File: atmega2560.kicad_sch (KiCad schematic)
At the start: 7 parts, among them SW1701 SW_SPST, U1701 ATmega2560-16A, U1702 HEADER_3x2, Y1701 crystal_arduino

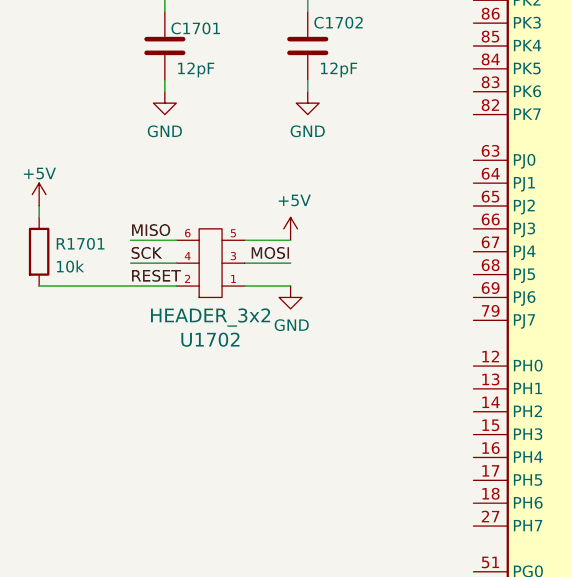
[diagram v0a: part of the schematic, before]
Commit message: added ch340.sch
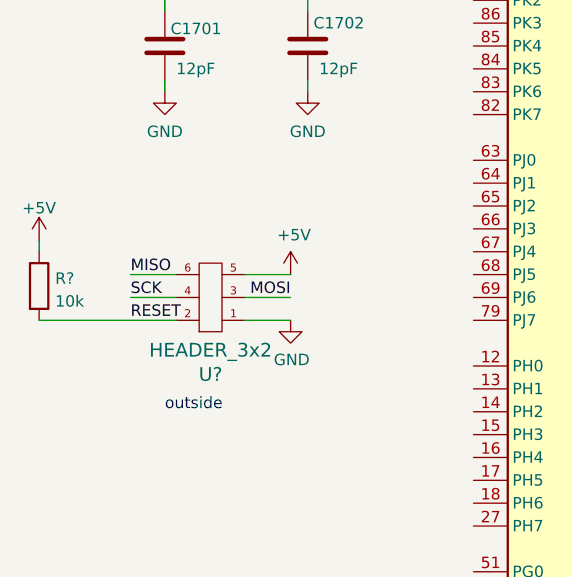
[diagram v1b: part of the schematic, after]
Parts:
- removed R1701: 10k, Resistor_SMD:R_1206_3216Metric_Pad1.30x1.75mm_HandSolder, symbol Device:R
- removed U1702: HEADER_3x2, Connector_PinSocket_1.27mm:PinSocket_2x03_P1.27mm_Vertical, symbol servoDriverSMD-rescue:HEADER_3x2-w_connectors
- added R?: 10k, Resistor_SMD:R_0603_1608Metric_Pad0.98x0.95mm_HandSolder, symbol Device:R
- added U?: HEADER_3x2, Connector_PinSocket_1.27mm:PinSocket_2x03_P1.27mm_Vertical, symbol servoDriverSMD-rescue:HEADER_3x2-w_connectors
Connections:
- net +5V: now also R?.1, U?.5
- net GND: now also U?.1
- net MISO: now also U?.6
- net MOSI: now also U?.3
- net RESET: now also R?.2, U?.2
- net SCK: now also U?.4
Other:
- note added: "outside"

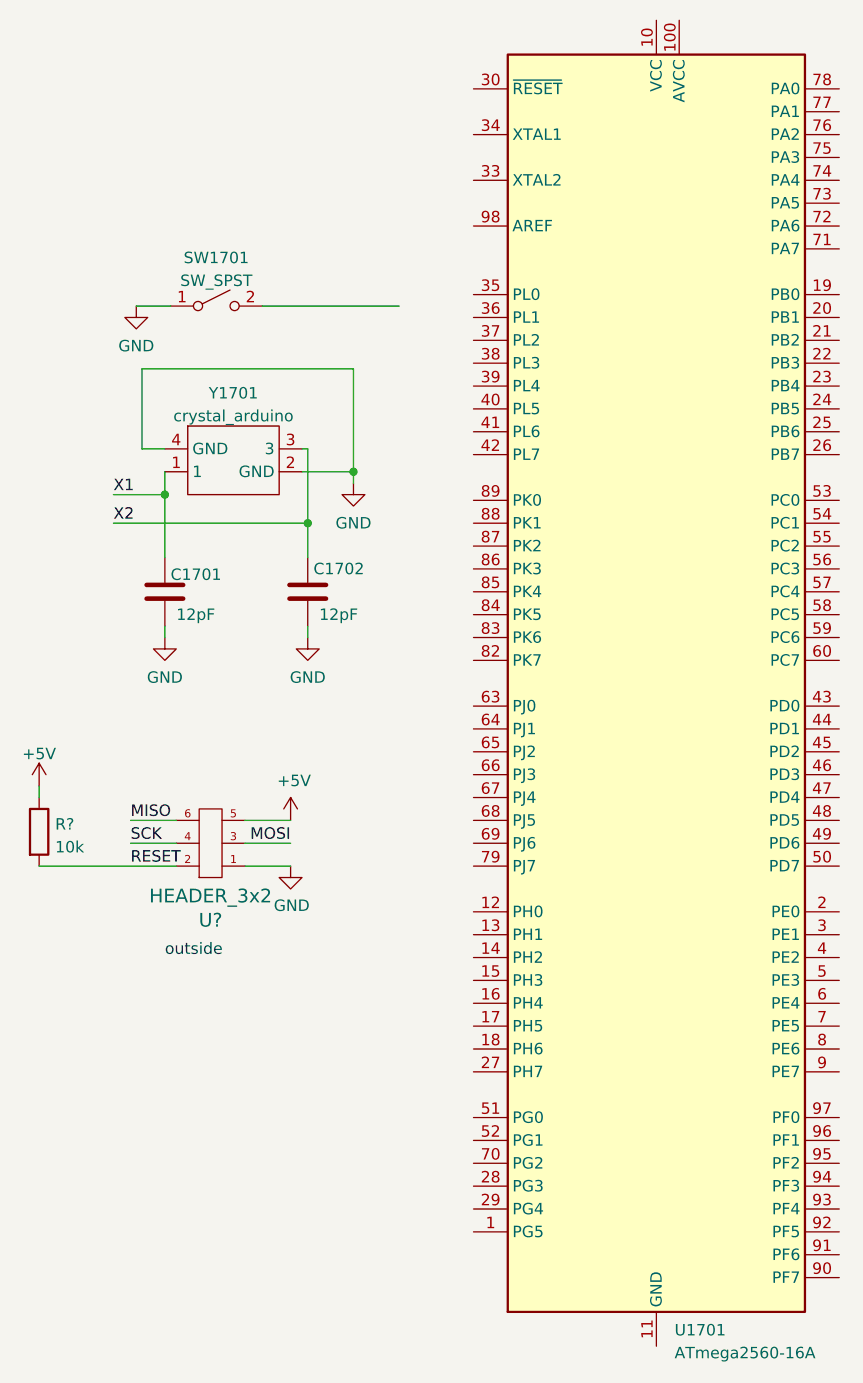
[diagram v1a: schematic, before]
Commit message: added hierarchial labels to some schematics
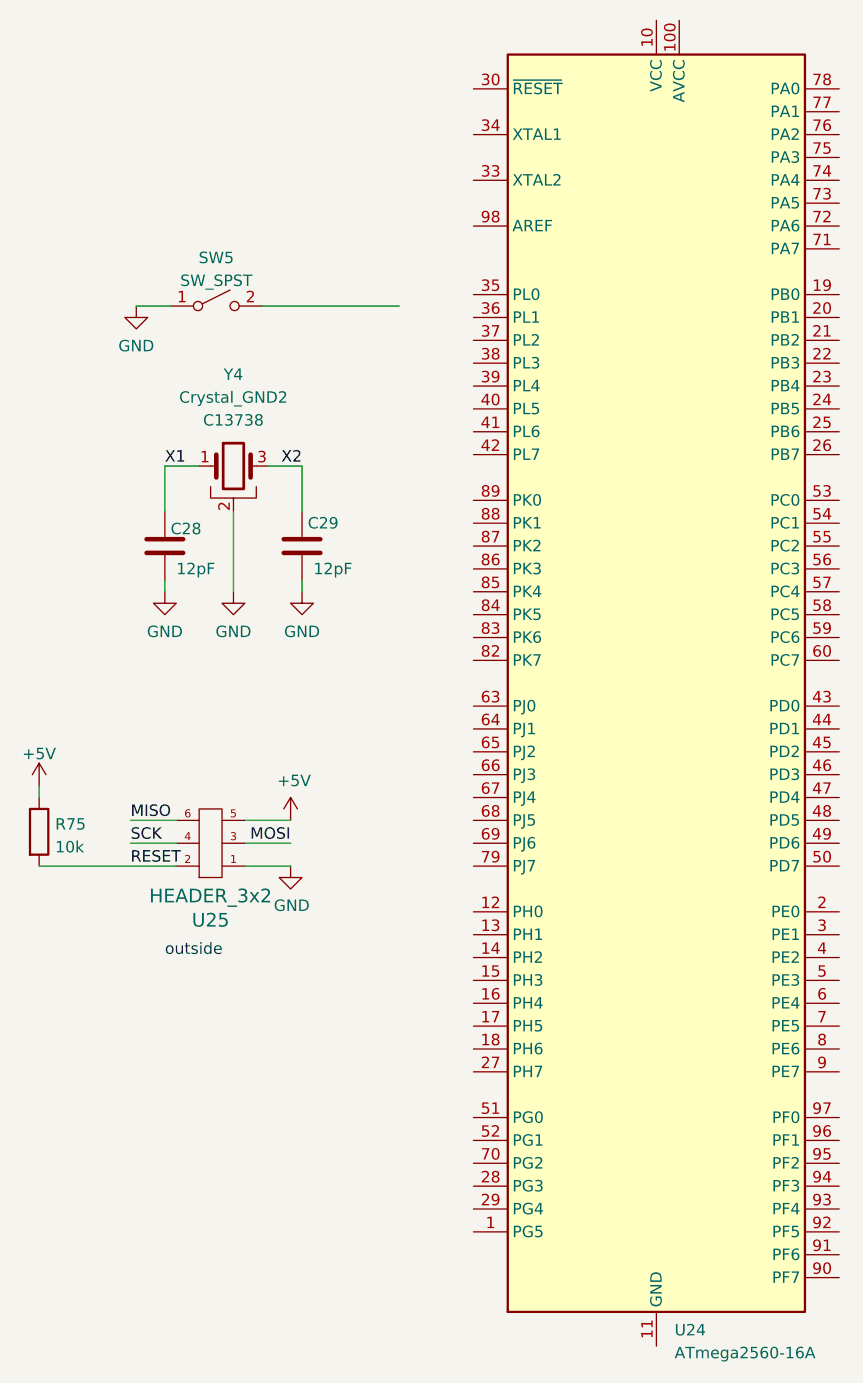
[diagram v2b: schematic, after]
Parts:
- removed Y1701: crystal_arduino, custom_kicad_lib_sk:crystal_arduino, symbol custom_bas:crystal_arduino
- added Y4: Crystal_GND2, custom_kicad_lib_sk:crystal_arduino, symbol custom_kicad_lib_sk:crystal_arduino
- gave numbers to parts that had none: 2
- renumbered C1701 to C28, C1702 to C29, SW1701 to SW5, U1701 to U24
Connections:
- net GND: now also Y4.2 (GND), Y4.4 (GND)
- net X1: now also Y4.1
- net X2: now also Y4.3
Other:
- moved on the sheet: C28, C29

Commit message: moved some schematic scheets to their own folders and routed a board with it. This allow for re-use of PCB parts.
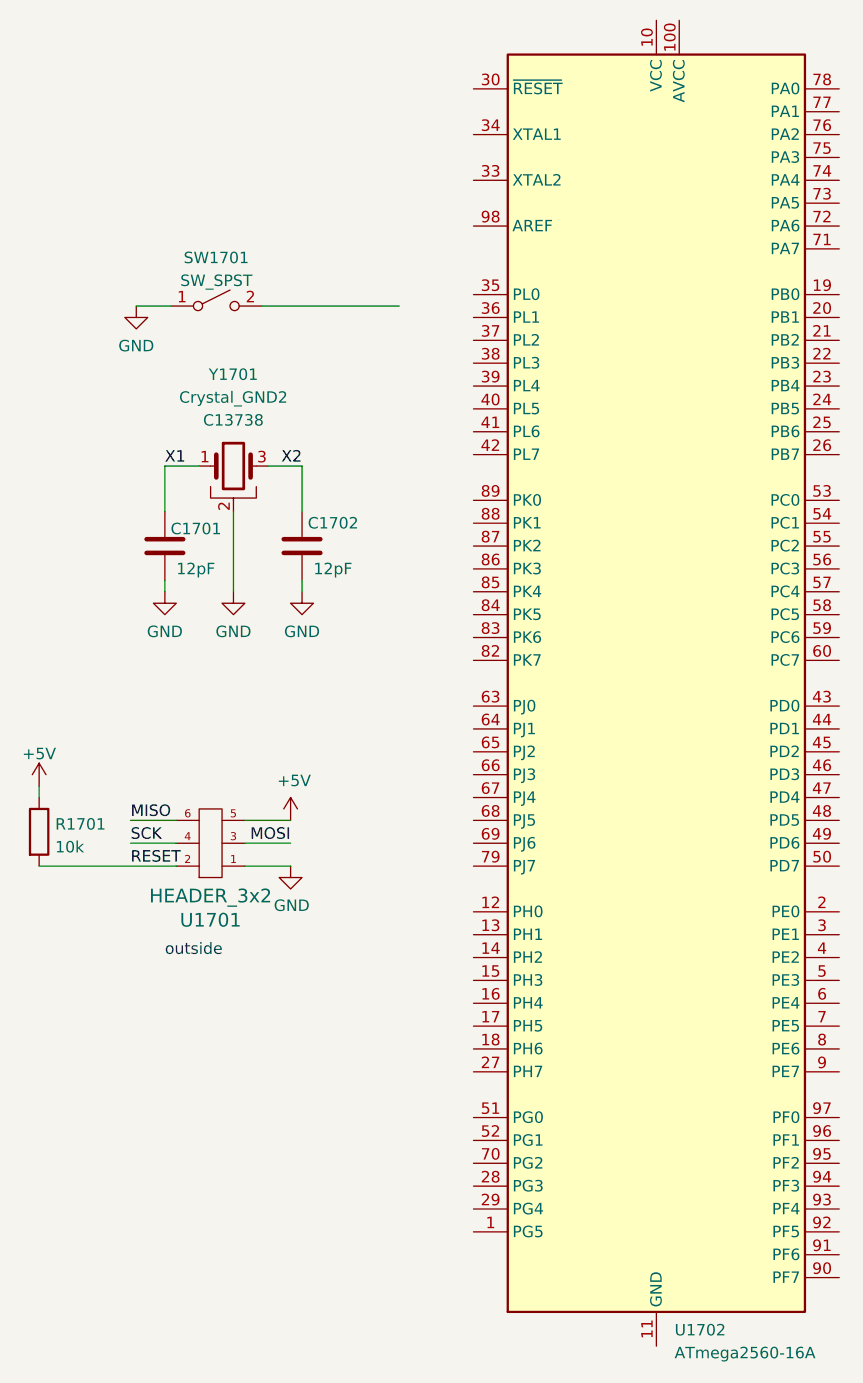
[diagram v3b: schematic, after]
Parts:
- renumbered C28 to C1701, C29 to C1702, R75 to R1701, SW5 to SW1701, U25 to U1701, U24 to U1702, Y4 to Y1701
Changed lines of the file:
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@@
   (symbol (lib_id "power:+5V") (at 48.26 111.76 0) (unit 1)
     (in_bom yes) (on_board yes) (dnp no) (fields_autoplaced)
-    (property "Reference" "#PWR070" (at 48.26 115.57 0)
+    (property "Reference" "#PWR0147" (at 48.26 115.57 0)
       (effects (font (size 1.27 1.27)) hide)
     )
@@
       (project "general_schematics"
         (path "/e777d9ec-d073-4229-a9e6-2cf85636e407/bccc2f0e-4293-4340-930b-a120cb08f970"
-          (reference "#PWR070") (unit 1)
+          (reference "#PWR0147") (unit 1)
         )
       )
@@
   (symbol (lib_id "Device:R") (at 48.26 116.84 0) (unit 1)
     (in_bom yes) (on_board yes) (dnp no) (fields_autoplaced)
-    (property "Reference" "R75" (at 50.038 116.0053 0)
+    (property "Reference" "R1701" (at 50.038 116.0053 0)
       (effects (font (size 1.27 1.27)) (justify left))
     )
@@
       (project "general_schematics"
         (path "/e777d9ec-d073-4229-a9e6-2cf85636e407/bccc2f0e-4293-4340-930b-a120cb08f970"
-          (reference "R75") (unit 1)
+          (reference "R1701") (unit 1)
         )
       )
@@
   (symbol (lib_id "power:GND") (at 77.47 90.17 0) (unit 1)
     (in_bom yes) (on_board yes) (dnp no)
-    (property "Reference" "#PWR069" (at 77.47 96.52 0)
+    (property "Reference" "#PWR0151" (at 77.47 96.52 0)
       (effects (font (size 1.27 1.27)) hide)
     )
@@
       (project "general_schematics"
         (path "/e777d9ec-d073-4229-a9e6-2cf85636e407/bccc2f0e-4293-4340-930b-a120cb08f970"
-          (reference "#PWR069") (unit 1)
+          (reference "#PWR0151") (unit 1)
         )
       )
@@
   (symbol (lib_id "servoDriverSMD-rescue:HEADER_3x2-w_connectors") (at 67.31 118.11 180) (unit 1)
     (in_bom yes) (on_board yes) (dnp no)
-    (property "Reference" "U25" (at 67.31 126.6698 0)
+    (property "Reference" "U1701" (at 67.31 126.6698 0)
       (effects (font (size 1.524 1.524)))
     )
@@
       (project "general_schematics"
         (path "/e777d9ec-d073-4229-a9e6-2cf85636e407/bccc2f0e-4293-4340-930b-a120cb08f970"
-          (reference "U25") (unit 1)
+          (reference "U1701") (unit 1)
         )
       )
@@
   (symbol (lib_id "power:GND") (at 76.2 120.65 0) (unit 1)
     (in_bom yes) (on_board yes) (dnp no)
-    (property "Reference" "#PWR072" (at 76.2 127 0)
+    (property "Reference" "#PWR0153" (at 76.2 127 0)
       (effects (font (size 1.27 1.27)) hide)
     )
@@
       (project "general_schematics"
         (path "/e777d9ec-d073-4229-a9e6-2cf85636e407/bccc2f0e-4293-4340-930b-a120cb08f970"
-          (reference "#PWR072") (unit 1)
+          (reference "#PWR0153") (unit 1)
         )
       )
@@
   (symbol (lib_id "power:GND") (at 62.23 90.17 0) (unit 1)
     (in_bom yes) (on_board yes) (dnp no) (fields_autoplaced)
-    (property "Reference" "#PWR068" (at 62.23 96.52 0)
+    (property "Reference" "#PWR0150" (at 62.23 96.52 0)
       (effects (font (size 1.27 1.27)) hide)
     )
@@
       (project "general_schematics"
         (path "/e777d9ec-d073-4229-a9e6-2cf85636e407/bccc2f0e-4293-4340-930b-a120cb08f970"
-          (reference "#PWR068") (unit 1)
+          (reference "#PWR0150") (unit 1)
         )
       )
@@
   (symbol (lib_id "MCU_Microchip_ATmega:ATmega2560-16A") (at 116.84 100.33 0) (unit 1)
     (in_bom yes) (on_board yes) (dnp no) (fields_autoplaced)
-    (property "Reference" "U24" (at 118.8594 172.2104 0)
+    (property "Reference" "U1702" (at 118.8594 172.2104 0)
       (effects (font (size 1.27 1.27)) (justify left))
     )
@@
       (project "general_schematics"
         (path "/e777d9ec-d073-4229-a9e6-2cf85636e407/bccc2f0e-4293-4340-930b-a120cb08f970"
-          (reference "U24") (unit 1)
+          (reference "U1702") (unit 1)
         )
       )
@@
   (symbol (lib_id "power:GND") (at 59.055 58.42 0) (unit 1)
     (in_bom yes) (on_board yes) (dnp no) (fields_autoplaced)
-    (property "Reference" "#PWR066" (at 59.055 64.77 0)
+    (property "Reference" "#PWR0148" (at 59.055 64.77 0)
       (effects (font (size 1.27 1.27)) hide)
     )
@@
       (project "general_schematics"
         (path "/e777d9ec-d073-4229-a9e6-2cf85636e407/bccc2f0e-4293-4340-930b-a120cb08f970"
-          (reference "#PWR066") (unit 1)
+          (reference "#PWR0148") (unit 1)
         )
       )
@@
   (symbol (lib_id "power:GND") (at 69.85 90.17 0) (unit 1)
     (in_bom yes) (on_board yes) (dnp no) (fields_autoplaced)
-    (property "Reference" "#PWR067" (at 69.85 96.52 0)
+    (property "Reference" "#PWR0149" (at 69.85 96.52 0)
       (effects (font (size 1.27 1.27)) hide)
     )
@@
       (project "general_schematics"
         (path "/e777d9ec-d073-4229-a9e6-2cf85636e407/bccc2f0e-4293-4340-930b-a120cb08f970"
-          (reference "#PWR067") (unit 1)
+          (reference "#PWR0149") (unit 1)
         )
       )
@@
   (symbol (lib_id "Device:C") (at 62.23 85.09 180) (unit 1)
     (in_bom yes) (on_board yes) (dnp no)
-    (property "Reference" "C28" (at 62.865 83.185 0)
+    (property "Reference" "C1701" (at 62.865 83.185 0)
       (effects (font (size 1.27 1.27)) (justify right))
     )
@@
       (project "general_schematics"
         (path "/e777d9ec-d073-4229-a9e6-2cf85636e407/bccc2f0e-4293-4340-930b-a120cb08f970"
-          (reference "C28") (unit 1)
+          (reference "C1701") (unit 1)
         )
       )
@@
   (symbol (lib_id "power:+5V") (at 76.2 115.57 0) (unit 1)
     (in_bom yes) (on_board yes) (dnp no)
-    (property "Reference" "#PWR071" (at 76.2 119.38 0)
+    (property "Reference" "#PWR0152" (at 76.2 119.38 0)
       (effects (font (size 1.27 1.27)) hide)
     )
@@
       (project "general_schematics"
         (path "/e777d9ec-d073-4229-a9e6-2cf85636e407/bccc2f0e-4293-4340-930b-a120cb08f970"
-          (reference "#PWR071") (unit 1)
+          (reference "#PWR0152") (unit 1)
         )
       )
@@
   (symbol (lib_id "Switch:SW_SPST") (at 67.945 58.42 0) (unit 1)
     (in_bom yes) (on_board yes) (dnp no) (fields_autoplaced)
-    (property "Reference" "SW5" (at 67.945 53.0692 0)
+    (property "Reference" "SW1701" (at 67.945 53.0692 0)
       (effects (font (size 1.27 1.27)))
     )
@@
       (project "general_schematics"
         (path "/e777d9ec-d073-4229-a9e6-2cf85636e407/bccc2f0e-4293-4340-930b-a120cb08f970"
-          (reference "SW5") (unit 1)
+          (reference "SW1701") (unit 1)
         )
       )
@@
   (symbol (lib_id "custom_kicad_lib_sk:crystal_arduino") (at 69.85 76.2 0) (unit 1)
     (in_bom yes) (on_board yes) (dnp no) (fields_autoplaced)
-    (property "Reference" "Y4" (at 69.85 66.04 0)
+    (property "Reference" "Y1701" (at 69.85 66.04 0)
       (effects (font (size 1.27 1.27)))
     )
@@
       (project "general_schematics"
         (path "/e777d9ec-d073-4229-a9e6-2cf85636e407/bccc2f0e-4293-4340-930b-a120cb08f970"
-          (reference "Y4") (unit 1)
+          (reference "Y1701") (unit 1)
         )
       )
@@
   (symbol (lib_id "Device:C") (at 77.47 85.09 180) (unit 1)
     (in_bom yes) (on_board yes) (dnp no)
-    (property "Reference" "C29" (at 78.105 82.55 0)
+    (property "Reference" "C1702" (at 78.105 82.55 0)
       (effects (font (size 1.27 1.27)) (justify right))
     )
@@
       (project "general_schematics"
         (path "/e777d9ec-d073-4229-a9e6-2cf85636e407/bccc2f0e-4293-4340-930b-a120cb08f970"
-          (reference "C29") (unit 1)
-        )
-      )
+          (reference "C1702") (unit 1)
+        )
+      )
